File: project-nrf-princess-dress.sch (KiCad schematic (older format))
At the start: 29 parts, among them J1 Conn_01x02_Female, J2 Conn_01x04_Female, J3 Conn_01x12_Female, J4 Conn_01x04_Female, J5 Conn_01x12_Female, J6 Conn_01x01_Female, J7 Conn_01x04_Female, J8 SM04B-SRSS-TB(LF)(SN), J9 Conn_01x01_Female, Q1 Q_PMOS_GSD, U1 TXU0204BQAR, U2 TXU0204BQAR, U3 TXU0204BQAR

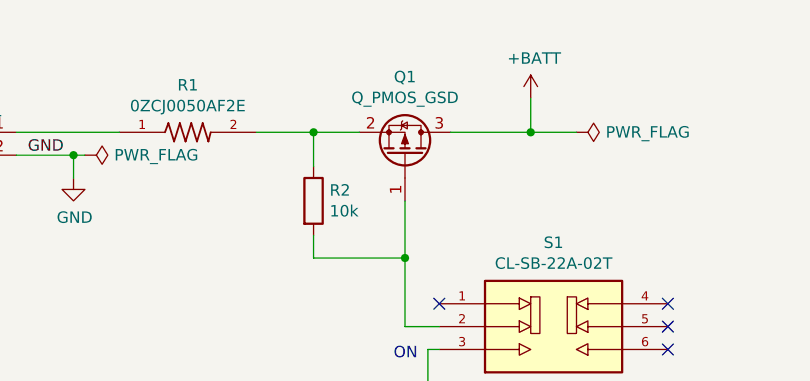
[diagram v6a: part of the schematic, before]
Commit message: Change the PMOS value
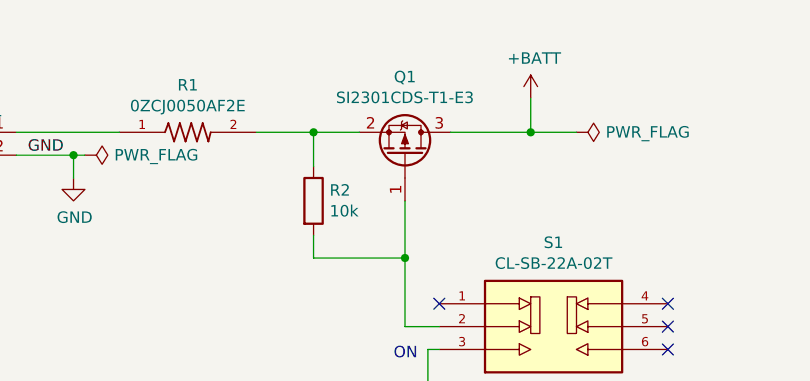
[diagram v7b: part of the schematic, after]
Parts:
- Q1: value Q_PMOS_GSD -> SI2301CDS-T1-E3
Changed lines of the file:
@@
 P 2650 1100
 F 0 "Q1" V 2992 1100 50  0000 C CNN
-F 1 "Q_PMOS_GSD" V 2901 1100 50  0000 C CNN
+F 1 "SI2301CDS-T1-E3" V 2901 1100 50  0000 C CNN
 F 2 "Package_TO_SOT_SMD:SOT-23" H 2850 1200 50  0001 C CNN
 F 3 "~" H 2650 1100 50  0001 C CNN
